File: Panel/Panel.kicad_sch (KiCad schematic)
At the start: 34 parts

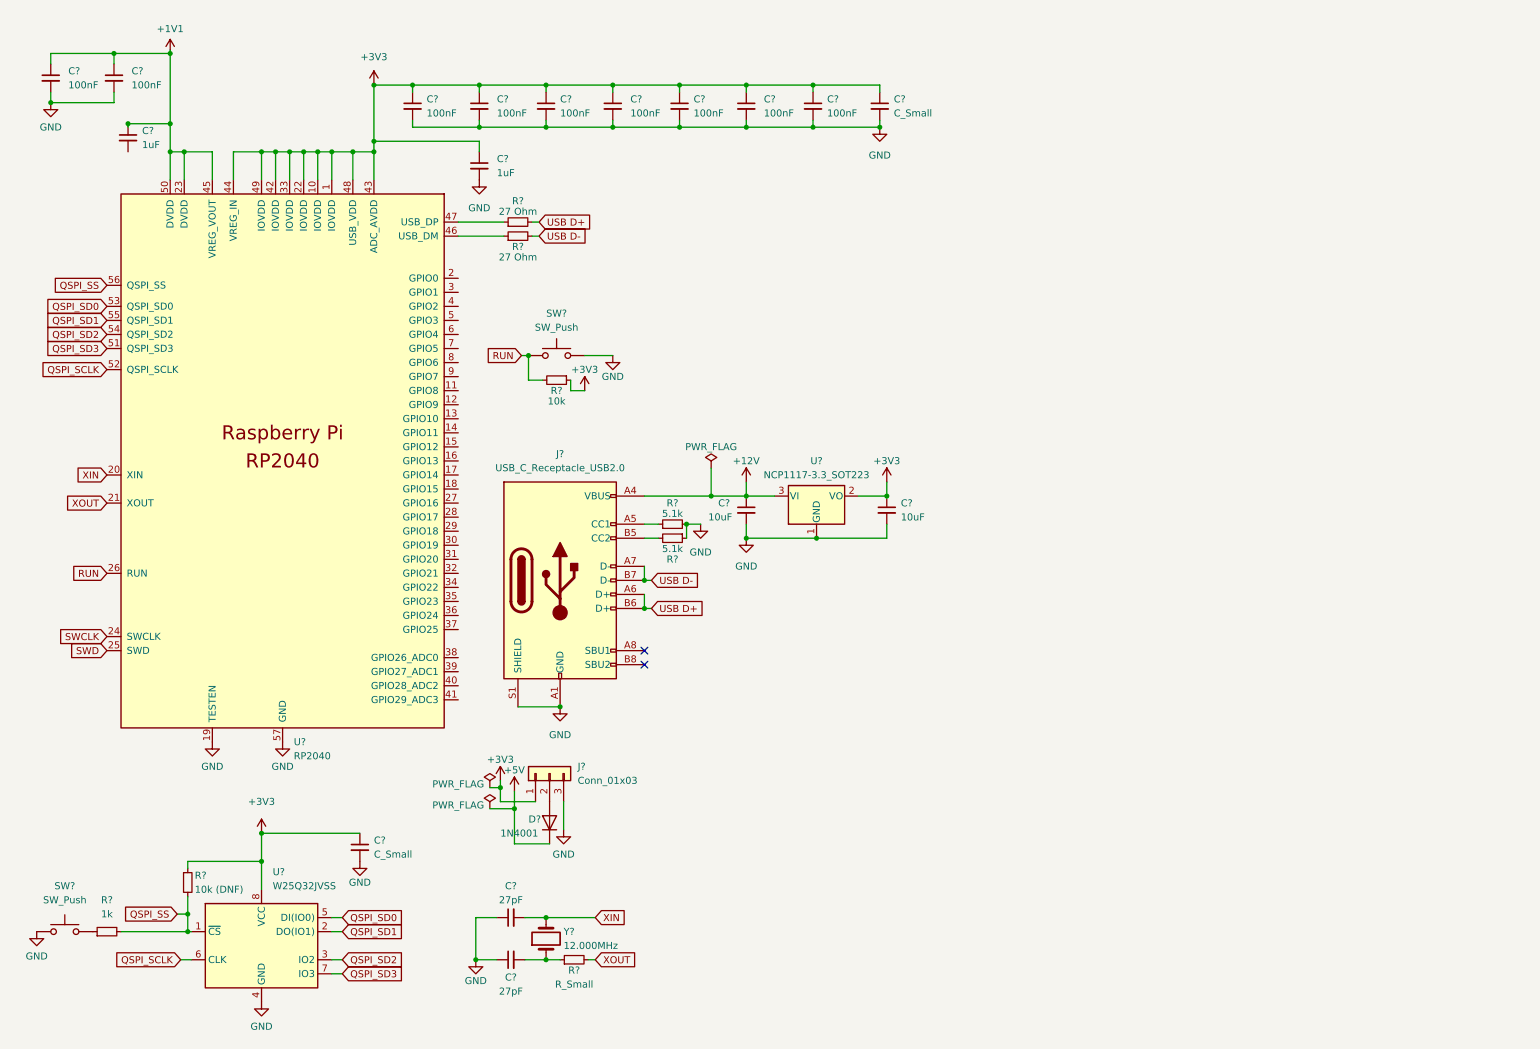
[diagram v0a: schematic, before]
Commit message: Initial component placement
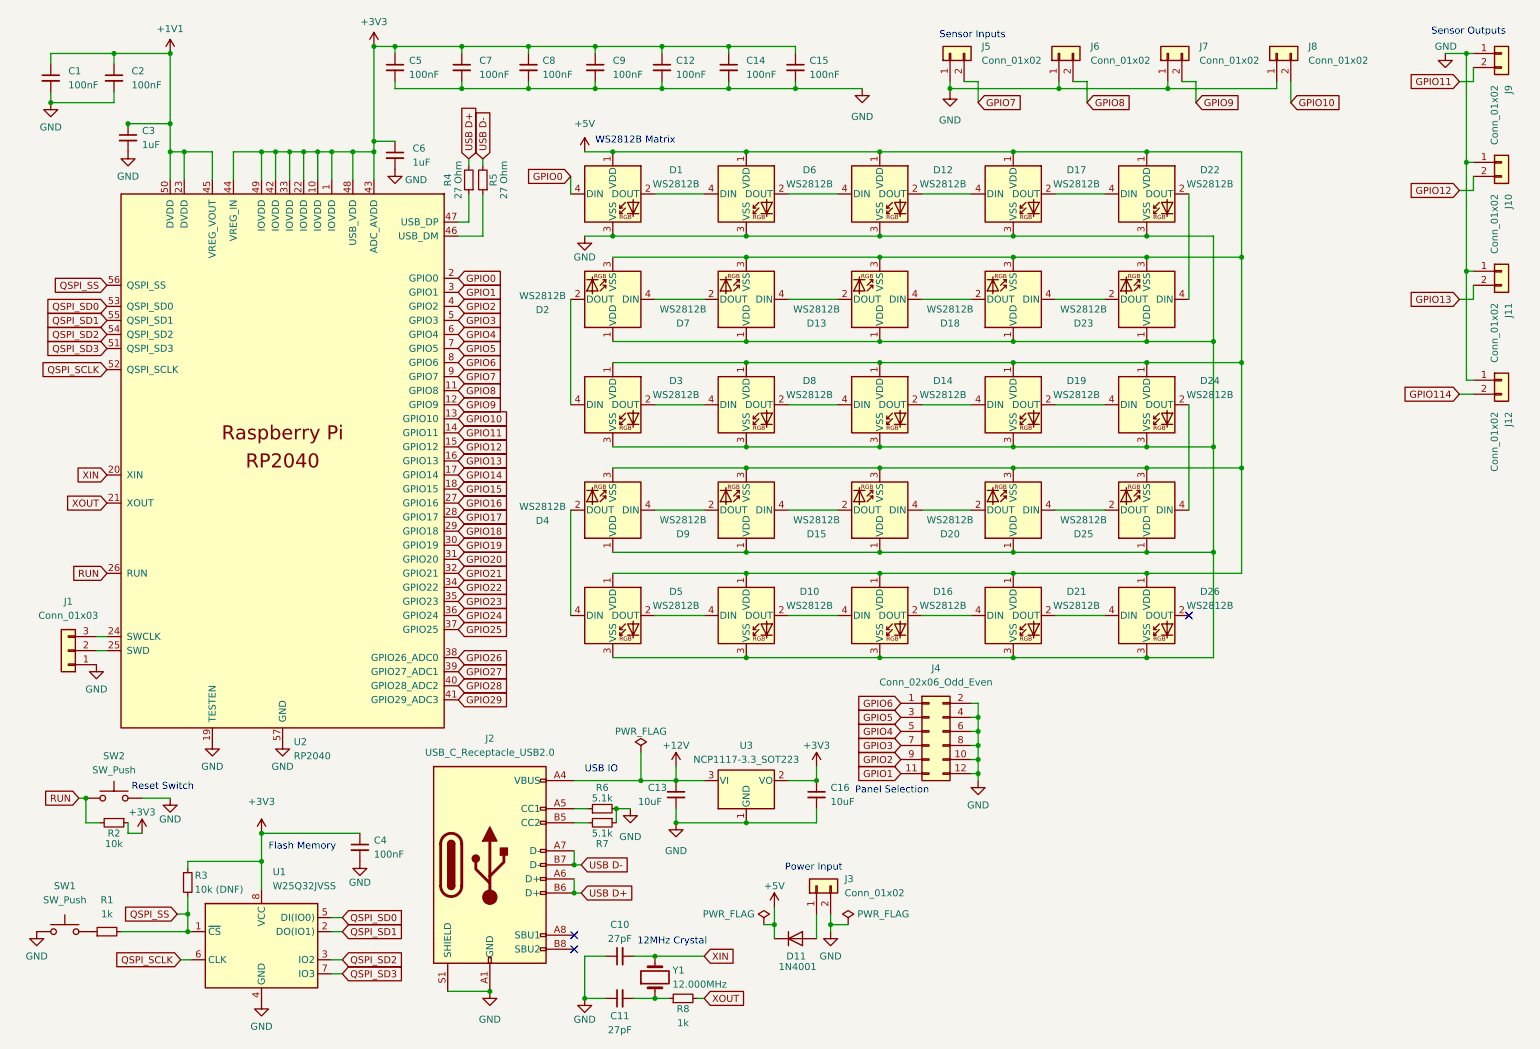
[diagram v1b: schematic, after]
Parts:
- removed C?: C_Small, symbol Device:C_Small
- removed J?: Conn_01x03, symbol Connector_Generic:Conn_01x03
- added D1, D10, D12, D13, D14, D15, D16, D17, D18, D19, D2, D20, D21, D22, D23, D24, D25, D26, D3, D4, D5, D6, D7, D8, D9: WS2812B, LED_SMD:LED_WS2812B_PLCC4_5.0x5.0mm_P3.2mm, symbol LED:WS2812B
- added J1: Conn_01x03, Connector_PinHeader_2.54mm:PinHeader_1x03_P2.54mm_Vertical, symbol Connector_Generic:Conn_01x03
- added J10, J11, J12, J5, J6, J7, J8, J9: Conn_01x02, Connector_Molex:Molex_Mini-Fit_Jr_5569-02A1_2x01_P4.20mm_Horizontal, symbol Connector_Generic:Conn_01x02
- added J3: Conn_01x02, Connector_JST:JST_XH_B2B-XH-AM_1x02_P2.50mm_Vertical, symbol Connector_Generic:Conn_01x02
- added J4: Conn_02x06_Odd_Even, Connector_PinHeader_2.54mm:PinHeader_2x06_P2.54mm_Vertical, symbol Connector_Generic:Conn_02x06_Odd_Even
- C1, C10, C11, C12, C13, C14, C15, C16, C2, C3, C5, C6, C7, C8, C9: renamed from C?; footprint (none) -> Capacitor_SMD:C_0504_1310Metric_Pad0.83x1.28mm_HandSolder
- C4: renamed from C?; value C_Small -> 100nF; footprint (none) -> Capacitor_SMD:C_0504_1310Metric_Pad0.83x1.28mm_HandSolder
- J2: renamed from J?; footprint (none) -> Connector_USB:USB_C_Receptacle_GCT_USB4085
- R1, R2, R3, R4, R5, R6, R7: renamed from R?; footprint (none) -> Resistor_SMD:R_0402_1005Metric_Pad0.72x0.64mm_HandSolder
- R8: renamed from R?; value R_Small -> 1k; footprint (none) -> Resistor_SMD:R_0402_1005Metric_Pad0.72x0.64mm_HandSolder
- SW1, SW2: renamed from SW?; footprint (none) -> Button_Switch_THT:SW_PUSH_6mm
- Y1: renamed from Y?; footprint (none) -> Crystal:Crystal_HC49-4H_Vertical
- gave numbers to parts that had none: 4
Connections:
- net +5V: now also D1.1 (VDD), D10.1 (VDD), D12.1 (VDD), D13.3 (VSS), D14.1 (VDD), D15.3 (VSS), D16.1 (VDD), D17.1 (VDD), D18.3 (VSS), D19.1 (VDD), D2.3 (VSS), D20.3 (VSS), D21.1 (VDD), D22.1 (VDD), D23.3 (VSS), D24.1 (VDD), D25.3 (VSS), D26.1 (VDD), D3.1 (VDD), D4.3 (VSS), D5.1 (VDD), D6.1 (VDD), D7.3 (VSS), D8.1 (VDD), D9.3 (VSS)
- net GND: now also C3.2, D1.3 (VSS), D10.3 (VSS), D12.3 (VSS), D13.1 (VDD), D14.3 (VSS), D15.1 (VDD), D16.3 (VSS), D17.3 (VSS), D18.1 (VDD), D19.3 (VSS), D2.1 (VDD), D20.1 (VDD), D21.3 (VSS), D22.3 (VSS), D23.1 (VDD), D24.3 (VSS), D25.1 (VDD), D26.3 (VSS), D3.3 (VSS), D4.1 (VDD), D5.3 (VSS), D6.3 (VSS), D7.1 (VDD), D8.3 (VSS), D9.1 (VDD), J1.1 (Pin_1), J10.1 (Pin_1), J11.1 (Pin_1), J12.1 (Pin_1), J3.2 (Pin_2), J4.10 (Pin_10), J4.12 (Pin_12), J4.2 (Pin_2), J4.4 (Pin_4), J4.6 (Pin_6), J4.8 (Pin_8), J5.1 (Pin_1), J6.1 (Pin_1), J7.1 (Pin_1), J8.1 (Pin_1), J9.1 (Pin_1)
- net at D11.2 (A): now also J3.1 (Pin_1)
- net GPIO8: now reaches U2.11 (GPIO8)
- net GPIO8: now also J6.2 (Pin_2)
- net GPIO9: now reaches U2.12 (GPIO9)
- net GPIO9: now also J7.2 (Pin_2)
- net GPIO10: now reaches U2.13 (GPIO10)
- net GPIO10: now also J8.2 (Pin_2)
- net GPIO11: now reaches U2.14 (GPIO11)
- net GPIO11: now also J9.2 (Pin_2)
- net GPIO12: now reaches U2.15 (GPIO12)
- net GPIO12: now also J10.2 (Pin_2)
- net GPIO13: now reaches U2.16 (GPIO13)
- net GPIO13: now also J11.2 (Pin_2)
- net GPIO14: now reaches U2.17 (GPIO14)
- net GPIO15: now reaches U2.18 (GPIO15)
- net GPIO0: now reaches U2.2 (GPIO0)
- net GPIO0: now also D1.4 (DIN)
- net GPIO16: now reaches U2.27 (GPIO16)
- net GPIO17: now reaches U2.28 (GPIO17)
- net GPIO18: now reaches U2.29 (GPIO18)
- net GPIO1: now reaches U2.3 (GPIO1)
- net GPIO1: now also J4.11 (Pin_11)
- net GPIO19: now reaches U2.30 (GPIO19)
- net GPIO20: now reaches U2.31 (GPIO20)
- net GPIO21: now reaches U2.32 (GPIO21)
- net GPIO22: now reaches U2.34 (GPIO22)
- net GPIO23: now reaches U2.35 (GPIO23)
- net GPIO24: now reaches U2.36 (GPIO24)
- net GPIO25: now reaches U2.37 (GPIO25)
- net GPIO26: now reaches U2.38 (GPIO26_ADC0)
- net GPIO27: now reaches U2.39 (GPIO27_ADC1)
- net GPIO2: now reaches U2.4 (GPIO2)
- net GPIO2: now also J4.9 (Pin_9)
- net GPIO28: now reaches U2.40 (GPIO28_ADC2)
- net GPIO29: now reaches U2.41 (GPIO29_ADC3)
- net GPIO3: now reaches U2.5 (GPIO3)
- net GPIO3: now also J4.7 (Pin_7)
- net GPIO4: now reaches U2.6 (GPIO4)
- net GPIO4: now also J4.5 (Pin_5)
- net GPIO5: now reaches U2.7 (GPIO5)
- net GPIO5: now also J4.3 (Pin_3)
- net GPIO6: now reaches U2.8 (GPIO6)
- net GPIO6: now also J4.1 (Pin_1)
- net GPIO7: now reaches U2.9 (GPIO7)
- net GPIO7: now also J5.2 (Pin_2)
- net SWCLK: no longer names the net of U2.24 (SWCLK)
- net SWCLK: now also J1.3 (Pin_3)
- net SWD: no longer names the net of U2.25 (SWD)
- net SWD: now also J1.2 (Pin_2)
- new net: D3.2 (DOUT), D8.4 (DIN)
- new net: D2.2 (DOUT), D3.4 (DIN)
- new net: D12.4 (DIN), D6.2 (DOUT)
- new net: D1.2 (DOUT), D6.4 (DIN)
- new net: D13.4 (DIN), D18.2 (DOUT)
- new net: D18.4 (DIN), D23.2 (DOUT)
- new net: D4.4 (DIN), D9.2 (DOUT)
- new net: D15.2 (DOUT), D9.4 (DIN)
- new net: D24.2 (DOUT), D25.4 (DIN)
- new net: D19.2 (DOUT), D24.4 (DIN)
- new net: D12.2 (DOUT), D17.4 (DIN)
- new net: D21.2 (DOUT), D26.4 (DIN)
- new net: D16.2 (DOUT), D21.4 (DIN)
- new net: D2.4 (DIN), D7.2 (DOUT)
- new net: D20.4 (DIN), D25.2 (DOUT)
- new net: D15.4 (DIN), D20.2 (DOUT)
- new net: D10.2 (DOUT), D16.4 (DIN)
- new net: D14.4 (DIN), D8.2 (DOUT)
- new net: D22.2 (DOUT), D23.4 (DIN)
- new net: D17.2 (DOUT), D22.4 (DIN)
- new net: D14.2 (DOUT), D19.4 (DIN)
- new net: D10.4 (DIN), D5.2 (DOUT)
- new net: D4.2 (DOUT), D5.4 (DIN)
- new net: D13.2 (DOUT), D7.4 (DIN)
- new net GPIO114: J12.2 (Pin_2)
- no-connect marks 2 -> 3
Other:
- note added: "12MHz Crystal"
- note added: "Flash Memory"
- note added: "Panel Selection"
- note added: "Power Input"
- note added: "Reset Switch"
- note added: "Sensor Inputs"
- note added: "Sensor Outputs"
- note added: "USB IO"
- note added: "WS2812B Matrix"
- moved on the sheet: C10, C11, C12, C13, C14, C15, C16, C5, C6, C7, C8, C9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

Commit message: 90% routed
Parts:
- removed J10, J11, J12, J5: Conn_01x02, Connector_Molex:Molex_Mini-Fit_Jr_5569-02A1_2x01_P4.20mm_Horizontal, symbol Connector_Generic:Conn_01x02
- added J5: Conn_01x07, 35312-XX60:35312-0760, symbol Connector_Generic:Conn_01x07
- J3: footprint Connector_JST:JST_XH_B2B-XH-AM_1x02_P2.50mm_Vertical -> Connector_JST:JST_XH_B2B-XH-A_1x02_P2.50mm_Vertical
- J6, J7, J8, J9: footprint Connector_Molex:Molex_Mini-Fit_Jr_5569-02A1_2x01_P4.20mm_Horizontal -> Connector_Molex:Molex_Mini-Fit_Jr_5569-02A2_2x01_P4.20mm_Horizontal
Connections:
- net +12V: now also J5.6 (Pin_6); no longer C13.1, J2.A4 (VBUS), J2.A9 (VBUS), J2.B4 (VBUS), J2.B9 (VBUS), U3.3 (VI)
- net +5V: now also C13.1, J2.A4 (VBUS), J2.A9 (VBUS), J2.B4 (VBUS), J2.B9 (VBUS), U3.3 (VI); no longer D1.1 (VDD), D10.1 (VDD), D12.1 (VDD), D13.3 (VSS), D14.1 (VDD), D15.3 (VSS), D16.1 (VDD), D17.1 (VDD), D18.3 (VSS), D19.1 (VDD), D2.3 (VSS), D20.3 (VSS), D21.1 (VDD), D22.1 (VDD), D23.3 (VSS), D24.1 (VDD), D25.3 (VSS), D26.1 (VDD), D3.1 (VDD), D4.3 (VSS), D5.1 (VDD), D6.1 (VDD), D7.3 (VSS), D8.1 (VDD), D9.3 (VSS)
- net GND: now also J5.7 (Pin_7)
- net GPIO10: no longer J8.2 (Pin_2)
- net GPIO11: no longer J9.2 (Pin_2)
- net GPIO8: no longer J6.2 (Pin_2)
- net GPIO9: no longer J7.2 (Pin_2)
- net Ext 5V: now reaches D11.2 (A), J3.1 (Pin_1)
- net Ext 5V: now also D1.1 (VDD), D10.1 (VDD), D12.1 (VDD), D13.3 (VSS), D14.1 (VDD), D15.3 (VSS), D16.1 (VDD), D17.1 (VDD), D18.3 (VSS), D19.1 (VDD), D2.3 (VSS), D20.3 (VSS), D21.1 (VDD), D22.1 (VDD), D23.3 (VSS), D24.1 (VDD), D25.3 (VSS), D26.1 (VDD), D3.1 (VDD), D4.3 (VSS), D5.1 (VDD), D6.1 (VDD), D7.3 (VSS), D8.1 (VDD), D9.3 (VSS)
- new net FRAME GND: J5.5 (Pin_5)
- new net SENSOR 1: J5.1 (Pin_1), J6.2 (Pin_2)
- new net SENSOR 2: J5.4 (Pin_4), J7.2 (Pin_2)
- new net SENSOR 3: J5.2 (Pin_2), J8.2 (Pin_2)
- new net SENSOR 4: J5.3 (Pin_3), J9.2 (Pin_2)
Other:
- note removed: "Sensor Outputs"
- moved on the sheet: C13, D1, D10, D11, D12, D13, D14, D15, D16, D17, D18, D19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

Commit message: Complete panel PCB
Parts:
- added J10: Conn_01x02, Connector_PinHeader_2.54mm:PinHeader_1x02_P2.54mm_Horizontal, symbol Connector_Generic:Conn_01x02
- added R10: 3.3k, Resistor_SMD:R_0402_1005Metric_Pad0.72x0.64mm_HandSolder, symbol Device:R_Small
- added R9: 8.9k, Resistor_SMD:R_0402_1005Metric_Pad0.72x0.64mm_HandSolder, symbol Device:R_Small
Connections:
- net GND: now also J10.1 (Pin_1), R10.2
- net GPIO7: now also R10.1, R9.2
- net SWDIO: now reaches J1.2 (Pin_2), U2.25 (SWD)
- net SWCLK: now reaches J1.3 (Pin_3), U2.24 (SWCLK)
- net +12V renamed LIGHT EN
- net LIGHT EN: now also J10.2 (Pin_2), R9.1
- net FRAME GND: no longer names the net of J5.5 (Pin_5)
- net GPIO10: no longer names the net of U2.13 (GPIO10)
- net GPIO11: no longer names the net of U2.14 (GPIO11)
- net GPIO12: no longer names the net of U2.15 (GPIO12)
- net GPIO13: no longer names the net of U2.16 (GPIO13)
- net GPIO14: no longer names the net of U2.17 (GPIO14)
- net GPIO15: no longer names the net of U2.18 (GPIO15)
- net GPIO16: no longer names the net of U2.27 (GPIO16)
- net GPIO17: no longer names the net of U2.28 (GPIO17)
- net GPIO18: no longer names the net of U2.29 (GPIO18)
- net GPIO19: no longer names the net of U2.30 (GPIO19)
- net GPIO20: no longer names the net of U2.31 (GPIO20)
- net GPIO21: no longer names the net of U2.32 (GPIO21)
- net GPIO22: no longer names the net of U2.34 (GPIO22)
- net GPIO23: no longer names the net of U2.35 (GPIO23)
- net GPIO24: no longer names the net of U2.36 (GPIO24)
- net GPIO25: no longer names the net of U2.37 (GPIO25)
- net GPIO26: no longer names the net of U2.38 (GPIO26_ADC0)
- net GPIO27: no longer names the net of U2.39 (GPIO27_ADC1)
- net GPIO28: no longer names the net of U2.40 (GPIO28_ADC2)
- net GPIO29: no longer names the net of U2.41 (GPIO29_ADC3)
- net GPIO8: no longer names the net of U2.11 (GPIO8)
- net GPIO9: no longer names the net of U2.12 (GPIO9)
- no-connect marks 3 -> 26
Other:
- moved on the sheet: C1, C12, C14, C15, C2, C3, C5, C6, C7, C8, C9, J1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

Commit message: Final Panel changes + first prod run gerber
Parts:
- added J11, J12: Conn_01x03, Connector_PinHeader_1.27mm:PinHeader_1x03_P1.27mm_Vertical, symbol Connector_Generic:Conn_01x03
- C1, C12, C14, C15, C2, C4, C5, C7, C8, C9: footprint Capacitor_SMD:C_0504_1310Metric_Pad0.83x1.28mm_HandSolder -> Capacitor_SMD:C_0402_1005Metric_Pad0.74x0.62mm_HandSolder; LCSC (none) -> C1525
- C10, C11: footprint Capacitor_SMD:C_0504_1310Metric_Pad0.83x1.28mm_HandSolder -> Capacitor_SMD:C_0402_1005Metric_Pad0.74x0.62mm_HandSolder; LCSC (none) -> C1557
- C13, C16: footprint Capacitor_SMD:C_0504_1310Metric_Pad0.83x1.28mm_HandSolder -> Capacitor_SMD:C_0402_1005Metric_Pad0.74x0.62mm_HandSolder; LCSC (none) -> C15525
- C3, C6: footprint Capacitor_SMD:C_0504_1310Metric_Pad0.83x1.28mm_HandSolder -> Capacitor_SMD:C_0402_1005Metric_Pad0.74x0.62mm_HandSolder; LCSC (none) -> C29266
- D1, D10, D12, D13, D14, D15, D16, D17, D18, D19, D2, D20, D21, D22, D23, D24, D25, D26, D3, D4, D5, D6, D7, D8, D9: LCSC (none) -> C114586
- J3: footprint Connector_JST:JST_XH_B2B-XH-A_1x02_P2.50mm_Vertical -> Connector_JST:JST_XH_S2B-XH-A-1_1x02_P2.50mm_Horizontal
- R1, R8: LCSC (none) -> C106235
- R10: value 3.3k -> 1k; LCSC (none) -> C106235
- R2: LCSC (none) -> C60490
- R3: value 10k (DNF) -> DNF
- R4, R5: LCSC (none) -> C2909343
- R6, R7: LCSC (none) -> C25905
- R9: value 8.9k -> 3k; LCSC (none) -> C321432
- U1: LCSC (none) -> C82344
- U2: LCSC (none) -> C2040
- U3: LCSC (none) -> C146799
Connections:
- net Ext 5V: now also J11.1 (Pin_1), J12.1 (Pin_1)
- net GND: now also J11.3 (Pin_3), J12.3 (Pin_3)
- net GPIO0: now also J12.2 (Pin_2)
- net at D26.2 (DOUT): now also J11.2 (Pin_2)
- no-connect marks 26 -> 25
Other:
- note added: "Just-in-case WS212B Output"
- note added: "Just-in-case WS2812B Input"

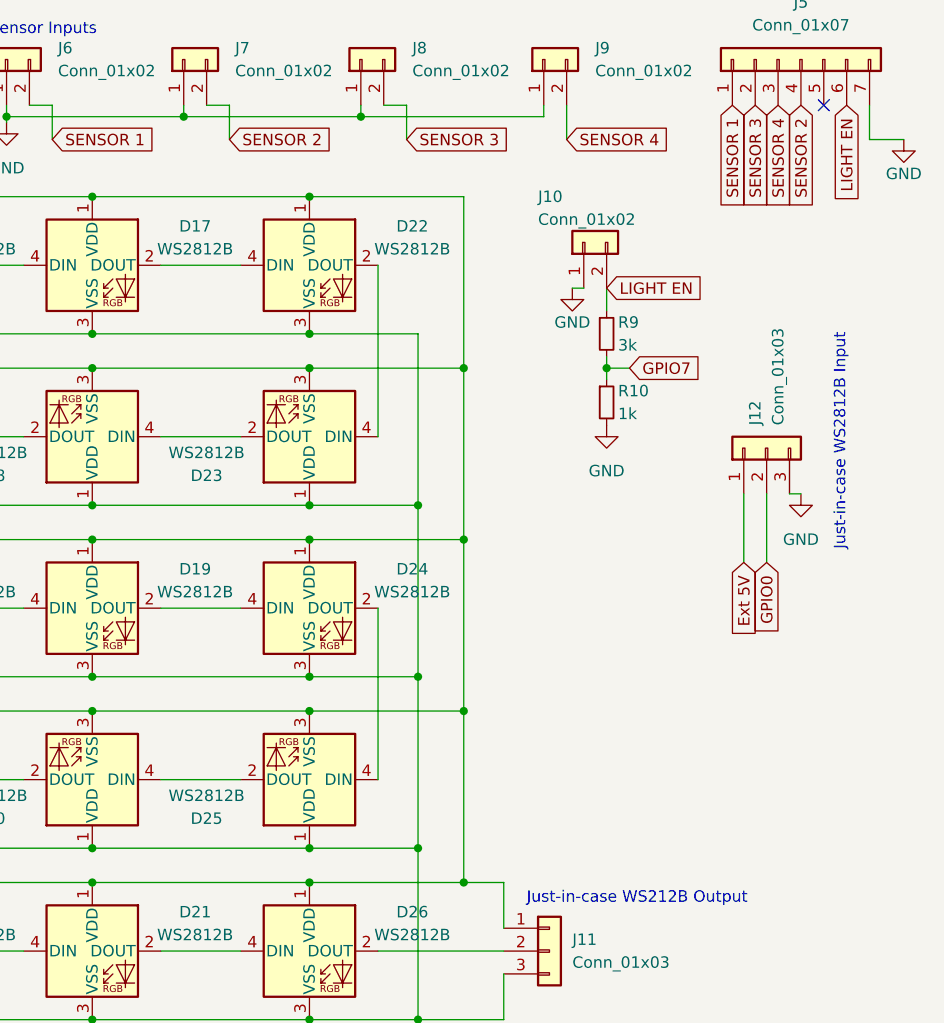
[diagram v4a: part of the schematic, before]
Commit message: Fix critical issue - KiCad assigned LED pins wrong
This would result in any boards manufactured with this design being unusable without cutting traces and bodging connections.
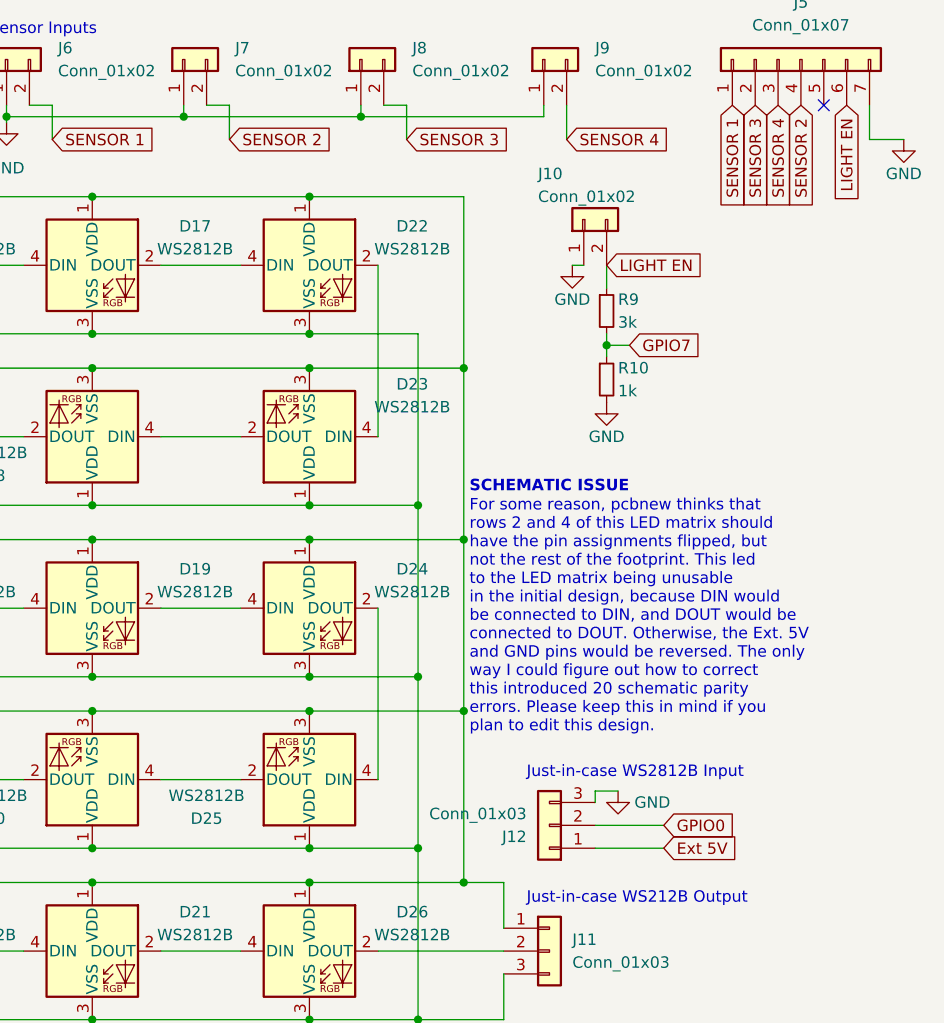
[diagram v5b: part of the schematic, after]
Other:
- note added: "For some reason, pcbnew thinks that rows 2 and 4 of this LED matrix should have the pin assignments flipped, but not the rest of the footprint. This led to the LED matrix being unusable in the initial design, because DIN would be connected to DIN, and DOUT would be connected to DOUT. Otherwise, the Ext. 5V and GND pins would be reversed. The only way I could figure out how to correct this introdu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"
- note added: "SCHEMATIC ISSUE"
- moved on the sheet: J10, J12, R10, R9

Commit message: Minor changes
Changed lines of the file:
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@@
   )
   (symbol (lib_id "Connector_Generic:Conn_01x03") (at 242.57 105.41 180) (unit 1)
-    (in_bom yes) (on_board yes) (fields_autoplaced)
-    (property "Reference" "J12" (id 0) (at 240.03 106.6801 0)
+    (in_bom yes) (on_board yes)
+    (property "Reference" "J12" (id 0) (at 236.22 99.06 90)
       (effects (font (size 1.27 1.27)) (justify left))
     )
-    (property "Value" "Conn_01x03" (id 1) (at 240.03 104.1401 0)
+    (property "Value" "Conn_01x03" (id 1) (at 238.76 99.06 90)
       (effects (font (size 1.27 1.27)) (justify left))
     )
